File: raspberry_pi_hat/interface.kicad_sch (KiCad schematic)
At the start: 9 parts, among them J1 LCD_screeen, J4 GPIO, J5 Switches, J6 LED_status

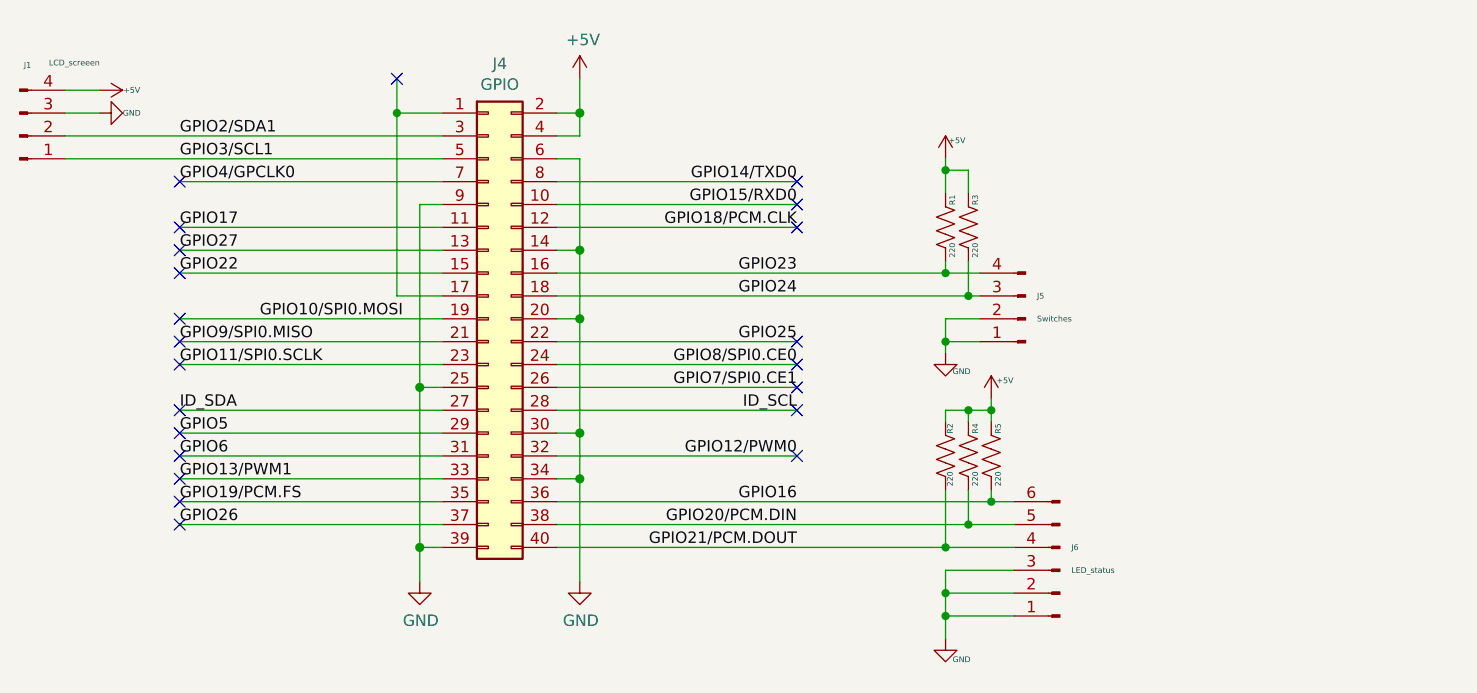
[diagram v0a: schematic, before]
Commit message: Solved split connection issues between boards
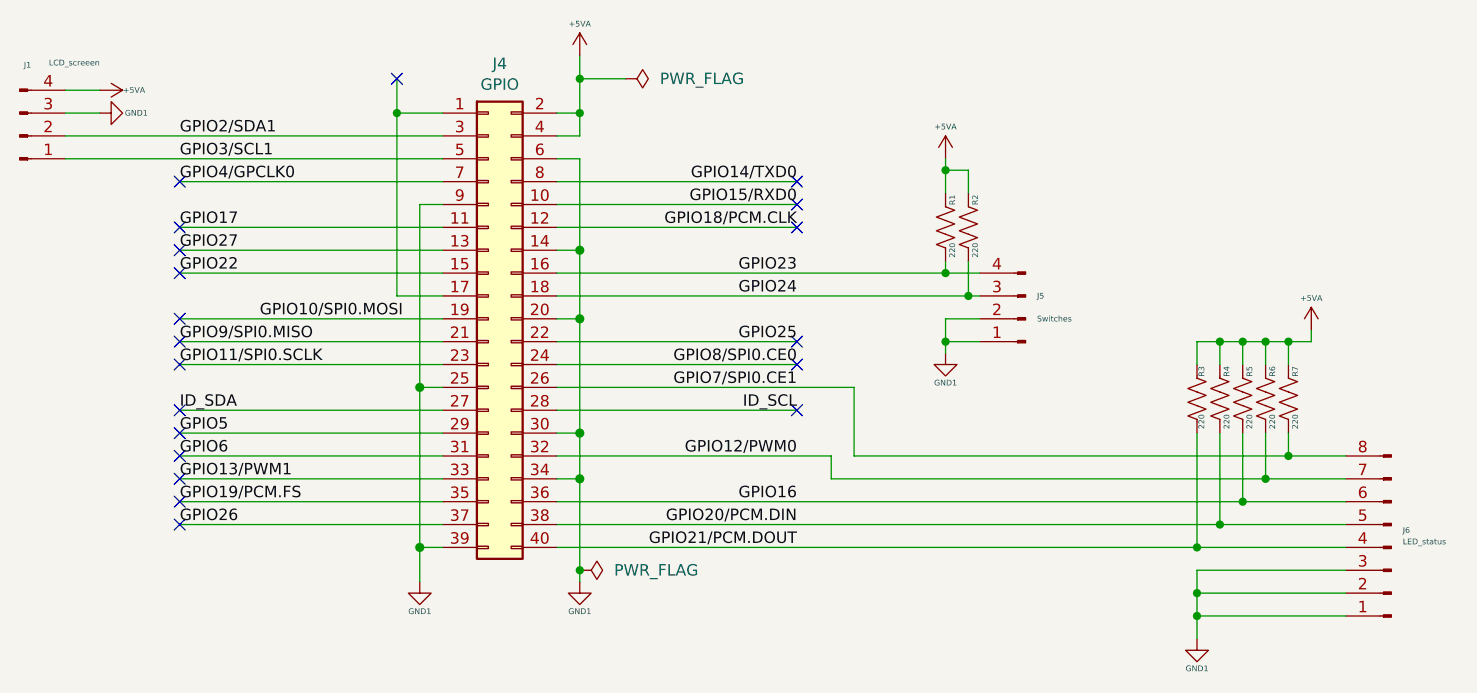
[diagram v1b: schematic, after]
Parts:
- removed J6: LED_status, Connector_Molex:Molex_KK-254_AE-6410-06A_1x06_P2.54mm_Vertical, symbol Connector:Conn_01x06_Pin
- added J6: LED_status, Connector_Molex:Molex_KK-254_AE-6410-08A_1x08_P2.54mm_Vertical, symbol Connector:Conn_01x08_Pin
- added R6, R7: 220, Resistor_THT:R_Axial_DIN0309_L9.0mm_D3.2mm_P12.70mm_Horizontal, symbol Device:R_US
- renumbered R3 to R2, R2 to R3
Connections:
- net GPIO12/PWM0: now also J6.7 (Pin_7), R6.2
- net GPIO16: now also J6.6 (Pin_6)
- net GPIO20/PCM.DIN: now also J6.5 (Pin_5)
- net GPIO21/PCM.DOUT: now also J6.4 (Pin_4)
- net GPIO7/SPI0.CE1: now also J6.8 (Pin_8), R7.2
- net +5V renamed +5VA
- net +5VA: now also R6.1, R7.1
- net GND renamed GND1
- net GND1: now also J6.1 (Pin_1), J6.2 (Pin_2), J6.3 (Pin_3)
- no-connect marks 22 -> 20
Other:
- moved on the sheet: R3, R4, R5

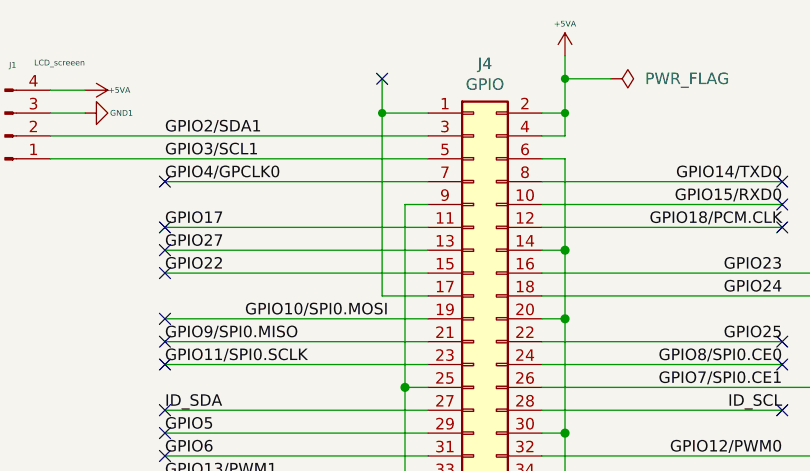
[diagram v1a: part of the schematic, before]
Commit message: Changed boards orientation and redistribution of components, still being 2 boards
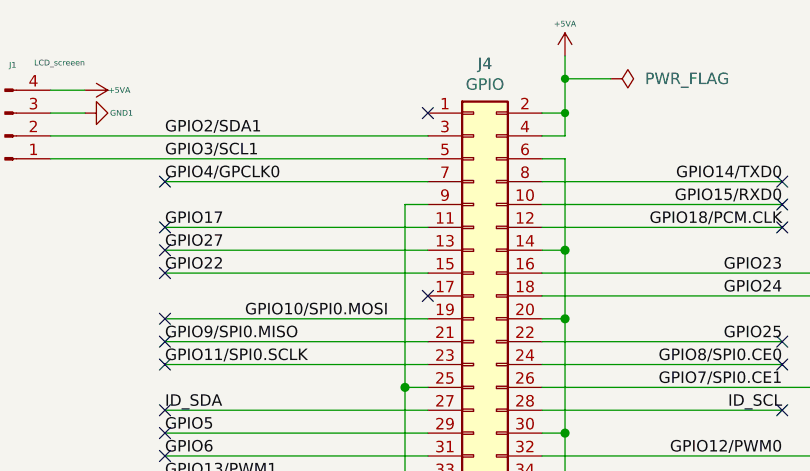
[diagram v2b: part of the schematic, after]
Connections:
- net at J4.1 (Pin_1): no longer J4.17 (Pin_17)
- no-connect marks 20 -> 21
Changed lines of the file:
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@@
-	)
-	(junction
-		(at 127 81.28)
-		(diameter 0)
-		(color 0 0 0 0)
 	)
 	(junction
@@
 	)
 	(no_connect
+		(at 132.08 81.28)
+	)
+	(no_connect
+		(at 132.08 101.6)
+	)
+	(no_connect
 		(at 102.87 106.68)
 	)
@@
 	)
 	(no_connect
-		(at 127 77.47)
-	)
-	(no_connect
 		(at 102.87 88.9)
 	)
@@
 	(wire
 		(pts
-			(xy 132.08 101.6) (xy 127 101.6)
-		)
-		(stroke
-			(width 0)
-			(type default)
-		)
-	)
-	(wire
-		(pts
 			(xy 102.87 124.46) (xy 132.08 124.46)
 		)
@@
 	(wire
 		(pts
-			(xy 127 101.6) (xy 127 81.28)
-		)
-		(stroke
-			(width 0)
-			(type default)
-		)
-	)
-	(wire
-		(pts
 			(xy 215.9 137.16) (xy 232.41 137.16)
 		)
@@
 	(wire
 		(pts
-			(xy 127 81.28) (xy 132.08 81.28)
-		)
-		(stroke
-			(width 0)
-			(type default)
-		)
-	)
-	(wire
-		(pts
 			(xy 220.98 124.46) (xy 232.41 124.46)
 		)
@@
 		)
 	)
-	(wire
-		(pts
-			(xy 127 81.28) (xy 127 77.47)
-		)
-		(stroke
-			(width 0)
-			(type default)
-		)
-	)
